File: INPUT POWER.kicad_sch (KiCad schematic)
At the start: 21 parts, among them J1 TYPE-C-31-M12_13, SW3 ON/OFF, U3 IP5306

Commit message: Screw Terminal FPs
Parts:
- U3: PN (none) -> IP5306
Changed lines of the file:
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@@
+      (effects (font (size 1.27 1.27)) hide)
+    )
+    (property "PN" "IP5306" (at 207.645 67.31 0)
       (effects (font (size 1.27 1.27)) hide)
     )

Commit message: Added LNA_IN Passives
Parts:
- L4: footprint (none) -> ESP32-S3_Dev_Board:L_0603_1608Metric; PN (none) -> LQM18PN1R0MFHD
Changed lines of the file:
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@@
       (effects (font (size 1.27 1.27)))
     )
-    (property "Footprint" "" (at 228.6 69.85 0)
+    (property "Footprint" "ESP32-S3_Dev_Board:L_0603_1608Metric" (at 228.6 69.85 0)
       (effects (font (size 1.27 1.27)) hide)
     )
@@
       (effects (font (size 1.27 1.27)) hide)
     )
+    (property "PN" "LQM18PN1R0MFHD" (at 228.6 69.85 0)
+      (effects (font (size 1.27 1.27)) hide)
+    )

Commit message: Instigated PCB Design
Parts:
- D2: PN (none) -> PRTR5V0U2X
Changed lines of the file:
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@@
       (effects (font (size 1.27 1.27)) (justify left top) hide)
+    )
+    (property "PN" "PRTR5V0U2X" (at 58.42 92.075 0)
+      (effects (font (size 1.27 1.27)) hide)
     )
     (pin "1")

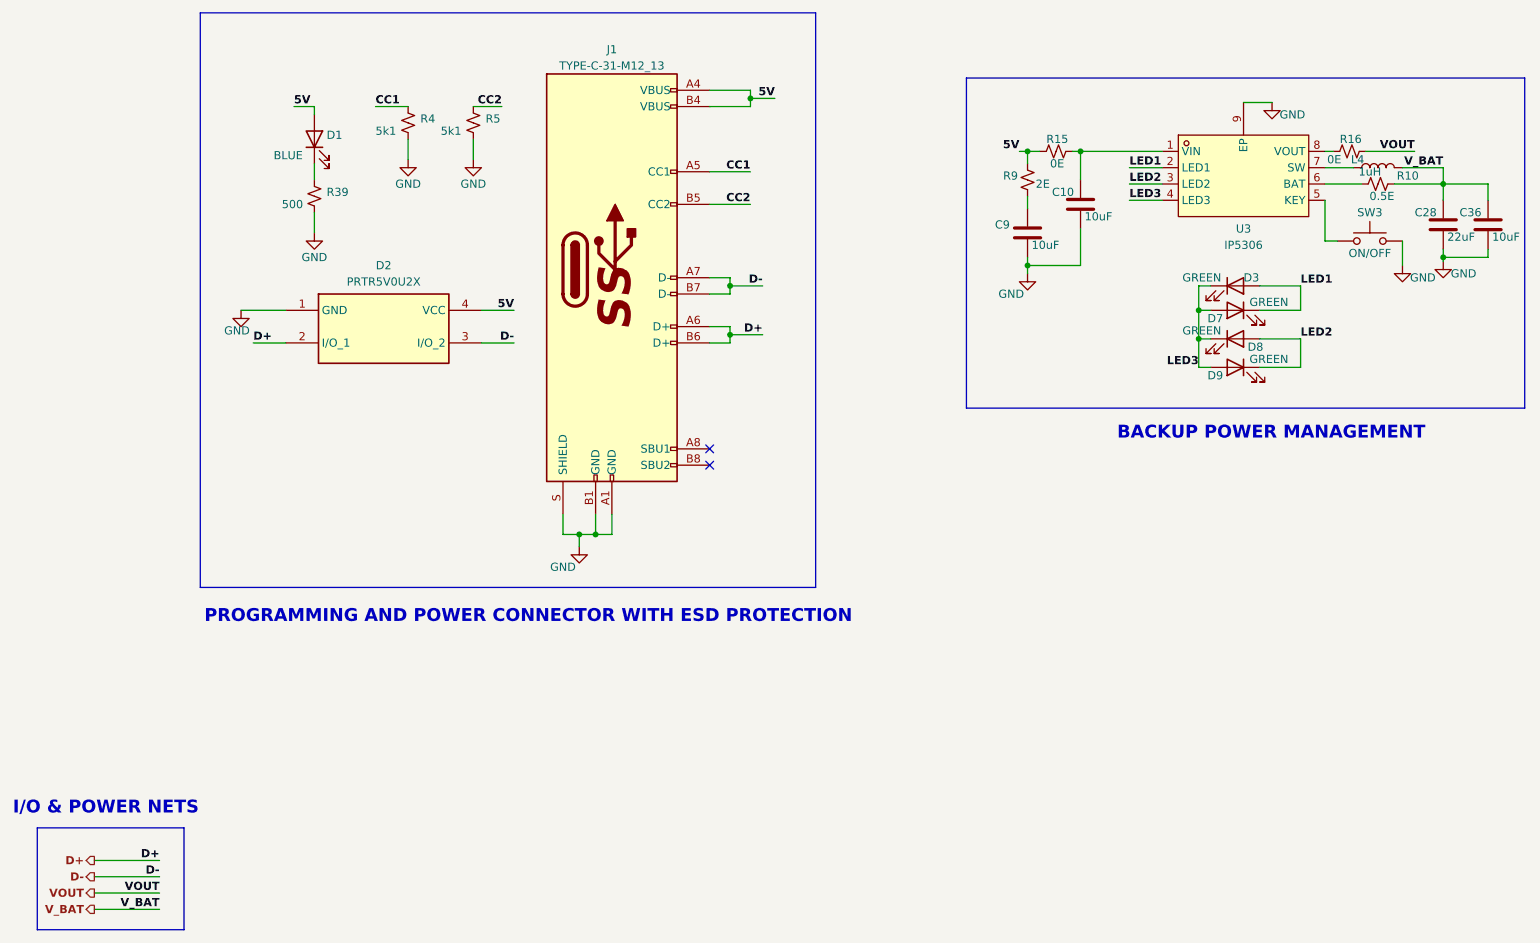
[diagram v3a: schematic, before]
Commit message: Arranged power section on PCB
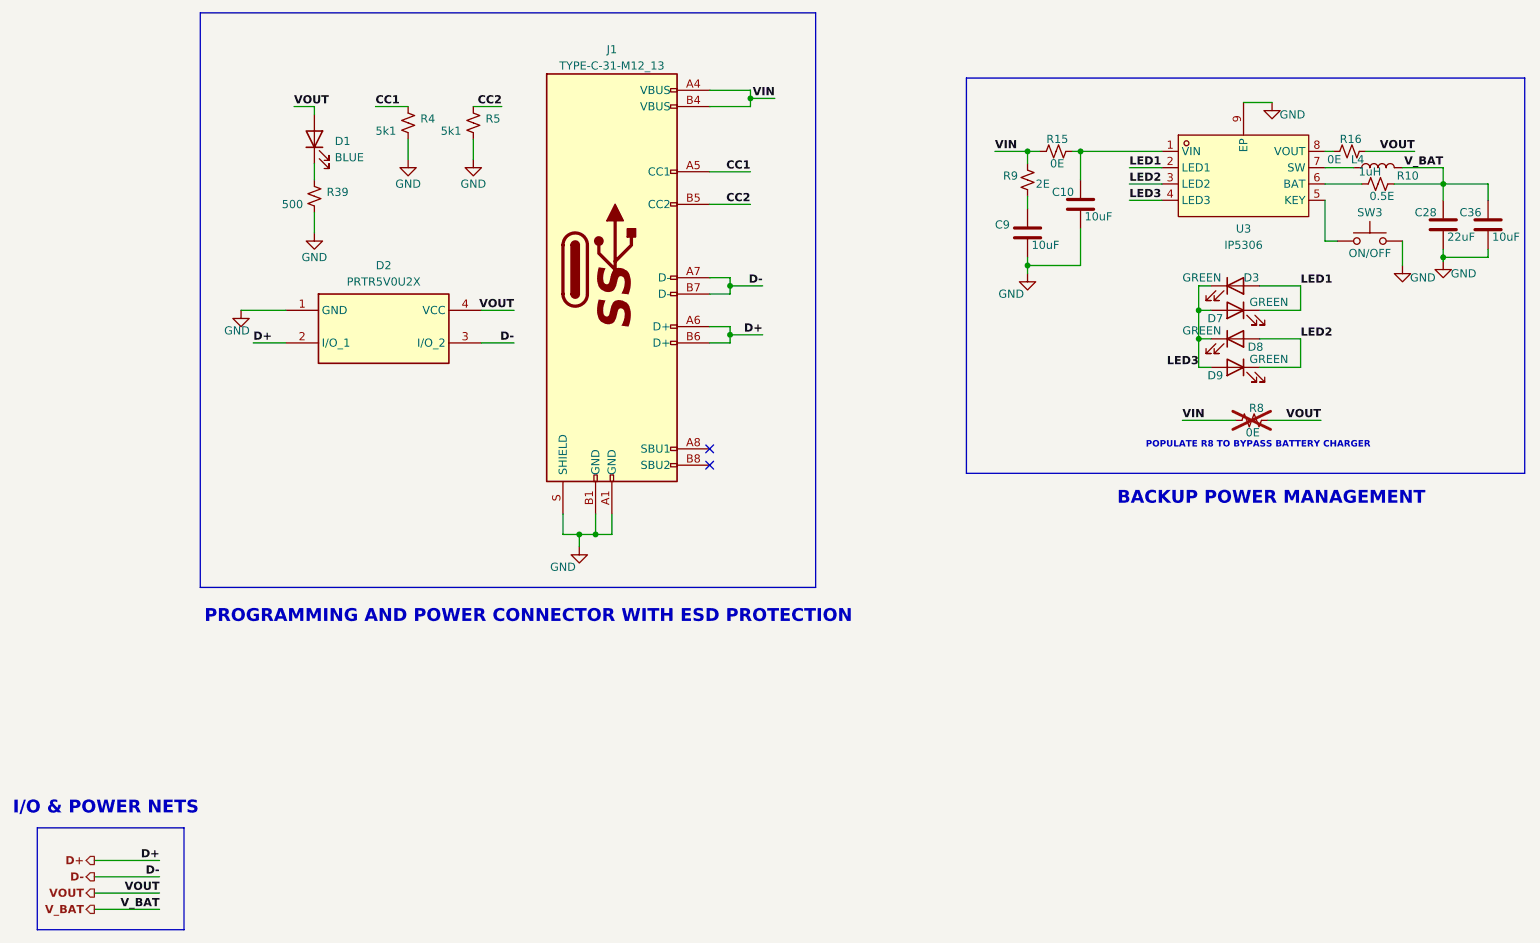
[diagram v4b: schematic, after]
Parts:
- added R8: 0E, ESP32-S3_Dev_Board:R_0603_1608Metric, symbol ESP32-S3_DB:R_Small_US
- D1: footprint ESP32-S3_DB:LED_0603_1608Metric -> ESP32-S3_Dev_Board:LED_0603_1608Metric
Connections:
- net VOUT: now also D1.2 (A), D2.4 (VCC), R8.2
- net 5V renamed VIN
- net VIN: now also R8.1; no longer D1.2 (A), D2.4 (VCC)
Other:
- note added: "POPULATE R8 TO BYPASS BATTERY CHARGER"
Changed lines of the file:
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@@
     (stroke (width 0) (type default))
   )
-  (bus (pts (xy 251.46 55.88) (xy 251.46 107.315))
+  (bus (pts (xy 251.46 55.88) (xy 251.46 117.475))
     (stroke (width 1) (type default) (color 72 72 72 1))
   )
@@
     (stroke (width 0) (type default))
   )
-  (bus (pts (xy 251.46 107.315) (xy 164.465 107.315))
+  (bus (pts (xy 251.46 117.475) (xy 164.465 117.475))
     (stroke (width 1) (type default) (color 72 72 72 1))
   )
@@
     (stroke (width 0) (type default))
   )
+  (wire (pts (xy 211.455 109.22) (xy 219.71 109.22))
+    (stroke (width 0) (type default))
+  )
   (wire (pts (xy 106.68 123.825) (xy 106.68 127))
     (stroke (width 0) (type default))
@@
   )
   (wire (pts (xy 38.735 185.42) (xy 28.575 185.42))
-    (stroke (width 0.5) (type default) (color 255 0 255 1))
+    (stroke (width 0.5) (type default) (color 132 132 0 1))
   )
   (wire (pts (xy 134.62 59.055) (xy 130.81 59.055))
@@
     (stroke (width 0) (type default))
   )
+  (wire (pts (xy 198.12 109.22) (xy 206.375 109.22))
+    (stroke (width 0) (type default))
+  )
   (wire (pts (xy 124.46 94.615) (xy 127.635 94.615))
     (stroke (width 0) (type default))
@@
     (stroke (width 0) (type default))
   )
-  (bus (pts (xy 164.465 55.88) (xy 164.465 107.315))
+  (bus (pts (xy 164.465 55.88) (xy 164.465 117.475))
     (stroke (width 1) (type default) (color 72 72 72 1))
   )
@@
     (stroke (width 0) (type default))
   )
-  (wire (pts (xy 172.72 67.31) (xy 173.99 67.31))
+  (wire (pts (xy 168.91 67.31) (xy 173.99 67.31))
     (stroke (width 0) (type default))
   )
@@
     (effects (font (size 2 2) bold (color 255 0 0 1)) (justify left bottom))
   )
-  (text "BACKUP POWER MANAGEMENT" (at 187.96 112.395 0)
+  (text "BACKUP POWER MANAGEMENT" (at 187.96 122.555 0)
     (effects (font (size 2 2) bold (color 255 0 0 1)) (justify left bottom))
+  )
+  (text "POPULATE R8 TO BYPASS BATTERY CHARGER" (at 192.405 113.665 0)
+    (effects (font (size 1 1) bold (color 0 0 255 1)) (justify left bottom))
   )
   (text "I/O & POWER NETS" (at 15.875 170.815 0)
@@
     (effects (font (size 1.27 1.27) bold (color 0 255 0 1)) (justify left bottom))
   )
+  (label "VOUT" (at 219.71 109.22 180) (fields_autoplaced)
+    (effects (font (size 1.27 1.27) bold (color 255 0 0 1)) (justify right bottom))
+  )
   (label "LED1" (at 189.865 69.85 0) (fields_autoplaced)
     (effects (font (size 1.27 1.27) bold (color 0 255 0 1)) (justify left bottom))
@@
   )
   (label "V_BAT" (at 38.735 185.42 180) (fields_autoplaced)
-    (effects (font (size 1.27 1.27) bold (color 255 0 255 1)) (justify right bottom))
-  )
-  (label "5V" (at 59.69 60.325 0) (fields_autoplaced)
+    (effects (font (size 1.27 1.27) bold (color 132 132 0 1)) (justify right bottom))
+  )
+  (label "VOUT" (at 59.69 60.325 0) (fields_autoplaced)
+    (effects (font (size 1.27 1.27) bold (color 255 0 0 1)) (justify left bottom))
+  )
+  (label "VOUT" (at 93.98 92.075 180) (fields_autoplaced)
+    (effects (font (size 1.27 1.27) bold (color 255 0 0 1)) (justify right bottom))
+  )
+  (label "VIN" (at 198.12 109.22 0) (fields_autoplaced)
     (effects (font (size 1.27 1.27) (thickness 0.254) bold (color 255 0 0 1)) (justify left bottom))
-  )
-  (label "5V" (at 172.72 67.31 180) (fields_autoplaced)
-    (effects (font (size 1.27 1.27) (thickness 0.254) bold (color 255 0 0 1)) (justify right bottom))
   )
   (label "D+" (at 53.34 97.155 0) (fields_autoplaced)
@@
     (effects (font (size 1.27 1.27) bold (color 255 0 0 1)) (justify right bottom))
   )
+  (label "VIN" (at 168.91 67.31 0) (fields_autoplaced)
+    (effects (font (size 1.27 1.27) (thickness 0.254) bold (color 255 0 0 1)) (justify left bottom))
+  )
   (label "D+" (at 38.735 177.8 180) (fields_autoplaced)
     (effects (font (size 1.27 1.27) (thickness 0.254) bold (color 0 0 255 1)) (justify right bottom))
@@
     (effects (font (size 1.27 1.27) (thickness 0.254) bold (color 255 153 0 1)) (justify left bottom))
   )
-  (label "5V" (at 93.98 92.075 180) (fields_autoplaced)
-    (effects (font (size 1.27 1.27) (thickness 0.254) bold (color 255 0 0 1)) (justify right bottom))
-  )
   (label "D-" (at 132.715 88.265 180) (fields_autoplaced)
     (effects (font (size 1.27 1.27) (thickness 0.254) bold (color 0 0 255 1)) (justify right bottom))
@@
     (effects (font (size 1.27 1.27) (thickness 0.254) bold (color 255 153 0 1)) (justify right bottom))
   )
-  (label "5V" (at 134.62 59.055 180) (fields_autoplaced)
+  (label "VIN" (at 134.62 59.055 180) (fields_autoplaced)
     (effects (font (size 1.27 1.27) (thickness 0.254) bold (color 255 0 0 1)) (justify right bottom))
   )
@@
   )
   (label "V_BAT" (at 238.76 69.85 180) (fields_autoplaced)
-    (effects (font (size 1.27 1.27) bold (color 255 0 255 1)) (justify right bottom))
+    (effects (font (size 1.27 1.27) bold (color 132 132 0 1)) (justify right bottom))
   )
   (label "D+" (at 132.715 95.885 180) (fields_autoplaced)
@@
   )
   (hierarchical_label "V_BAT" (shape output) (at 28.575 185.42 180) (fields_autoplaced)
-    (effects (font (size 1.27 1.27) bold (color 255 0 255 1)) (justify right))
+    (effects (font (size 1.27 1.27) bold (color 132 132 0 1)) (justify right))
   )
   (hierarchical_label "VOUT" (shape output) (at 28.575 182.88 180) (fields_autoplaced)
@@
         (path "/b7fc4bd3-c219-4455-832b-8d795385dcf1/95090a63-7b3c-4ea0-92b8-aeafe05264cd"
           (reference "#PWR053") (unit 1)
+        )
+      )
+    )
+  )
+  (symbol (lib_id "ESP32-S3_DB:LED") (at 62.865 65.405 90) (unit 1)
+    (in_bom yes) (on_board yes) (dnp no) (fields_autoplaced)
+    (property "Reference" "D1" (at 66.04 65.7225 90)
+      (effects (font (size 1.27 1.27)) (justify right))
+    )
+    (property "Value" "BLUE" (at 66.04 68.2625 90)
+      (effects (font (size 1.27 1.27)) (justify right))
+    )
+    (property "Footprint" "ESP32-S3_Dev_Board:LED_0603_1608Metric" (at 62.865 65.405 0)
+      (effects (font (size 1.27 1.27)) hide)
+    )
+    (property "Datasheet" "~" (at 62.865 65.405 0)
+      (effects (font (size 1.27 1.27)) hide)
+    )
+    (property "PN" "NCD0603B1" (at 62.865 65.405 90)
+      (effects (font (size 1.27 1.27)) hide)
+    )
+    (pin "1")
+    (pin "2")
+    (instances
+      (project "ESP32-S3_DB"
+        (path "/b7fc4bd3-c219-4455-832b-8d795385dcf1/95090a63-7b3c-4ea0-92b8-aeafe05264cd"
+          (reference "D1") (unit 1)
         )
       )
@@
         (path "/b7fc4bd3-c219-4455-832b-8d795385dcf1/95090a63-7b3c-4ea0-92b8-aeafe05264cd"
           (reference "C36") (unit 1)
+        )
+      )
+    )
+  )
+  (symbol (lib_id "ESP32-S3_DB:R_Small_US") (at 208.915 109.22 90) (unit 1)
+    (in_bom no) (on_board yes) (dnp yes)
+    (property "Reference" "R8" (at 210.82 107.315 90)
+      (effects (font (size 1.27 1.27)) (justify left))
+    )
+    (property "Value" "0E" (at 210.185 111.125 90)
+      (effects (font (size 1.27 1.27)) (justify left))
+    )
+    (property "Footprint" "ESP32-S3_Dev_Board:R_0603_1608Metric" (at 208.915 109.22 0)
+      (effects (font (size 1.27 1.27)) hide)
+    )
+    (property "Datasheet" "~" (at 208.915 109.22 0)
+      (effects (font (size 1.27 1.27)) hide)
+    )
+    (property "PN" "RC0603JR-070RL" (at 208.915 109.22 0)
+      (effects (font (size 1.27 1.27)) hide)
+    )
+    (pin "1")
+    (pin "2")
+    (instances
+      (project "ESP32-S3_DB"
+        (path "/b7fc4bd3-c219-4455-832b-8d795385dcf1/95090a63-7b3c-4ea0-92b8-aeafe05264cd"
+          (reference "R8") (unit 1)
         )
       )
@@
         )
       )
-    )
-  )
-  (symbol (lib_id "ESP32-S3_DB:LED") (at 62.865 65.405 90) (unit 1)
-    (in_bom yes) (on_board yes) (dnp no)
-    (property "Reference" "D1" (at 64.77 64.77 90)
-      (effects (font (size 1.27 1.27)) (justify right))
-    )
-    (property "Value" "BLUE" (at 56.515 67.945 90)
-      (effects (font (size 1.27 1.27)) (justify right))
-    )
-    (property "Footprint" "ESP32-S3_DB:LED_0603_1608Metric" (at 62.865 65.405 0)
-      (effects (font (size 1.27 1.27)) hide)
-    )
-    (property "Datasheet" "~" (at 62.865 65.405 0)
-      (effects (font (size 1.27 1.27)) hide)
-    )
-    (property "PN" "NCD0603B1" (at 62.865 65.405 0)
-      (effects (font (size 1.27 1.27)) hide)
-    )
-    (pin "1")
-    (pin "2")
-    (instances
-      (project "ESP32-S3_DB"
-        (path "/b7fc4bd3-c219-4455-832b-8d795385dcf1/95090a63-7b3c-4ea0-92b8-aeafe05264cd"
-          (reference "D1") (unit 1)
-        )
-      )
